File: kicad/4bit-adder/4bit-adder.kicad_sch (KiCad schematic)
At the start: 1 part, among them K1 SR11-5V-200-2C

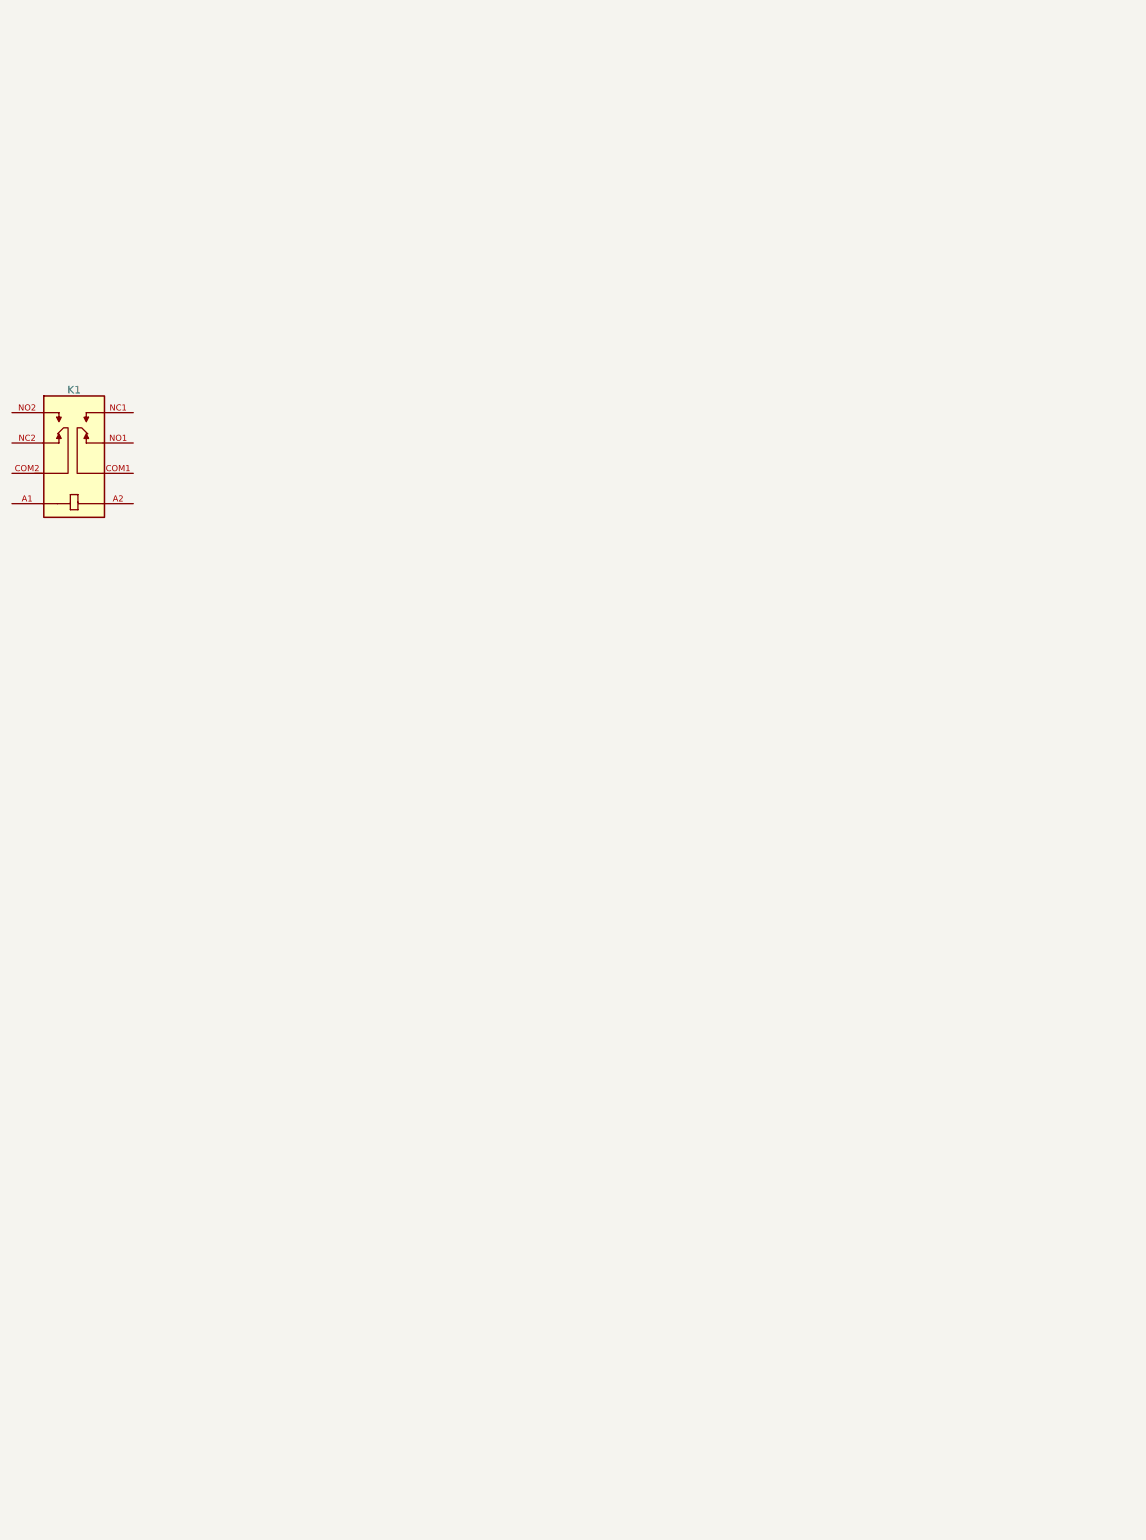
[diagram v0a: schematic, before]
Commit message: half adder schema
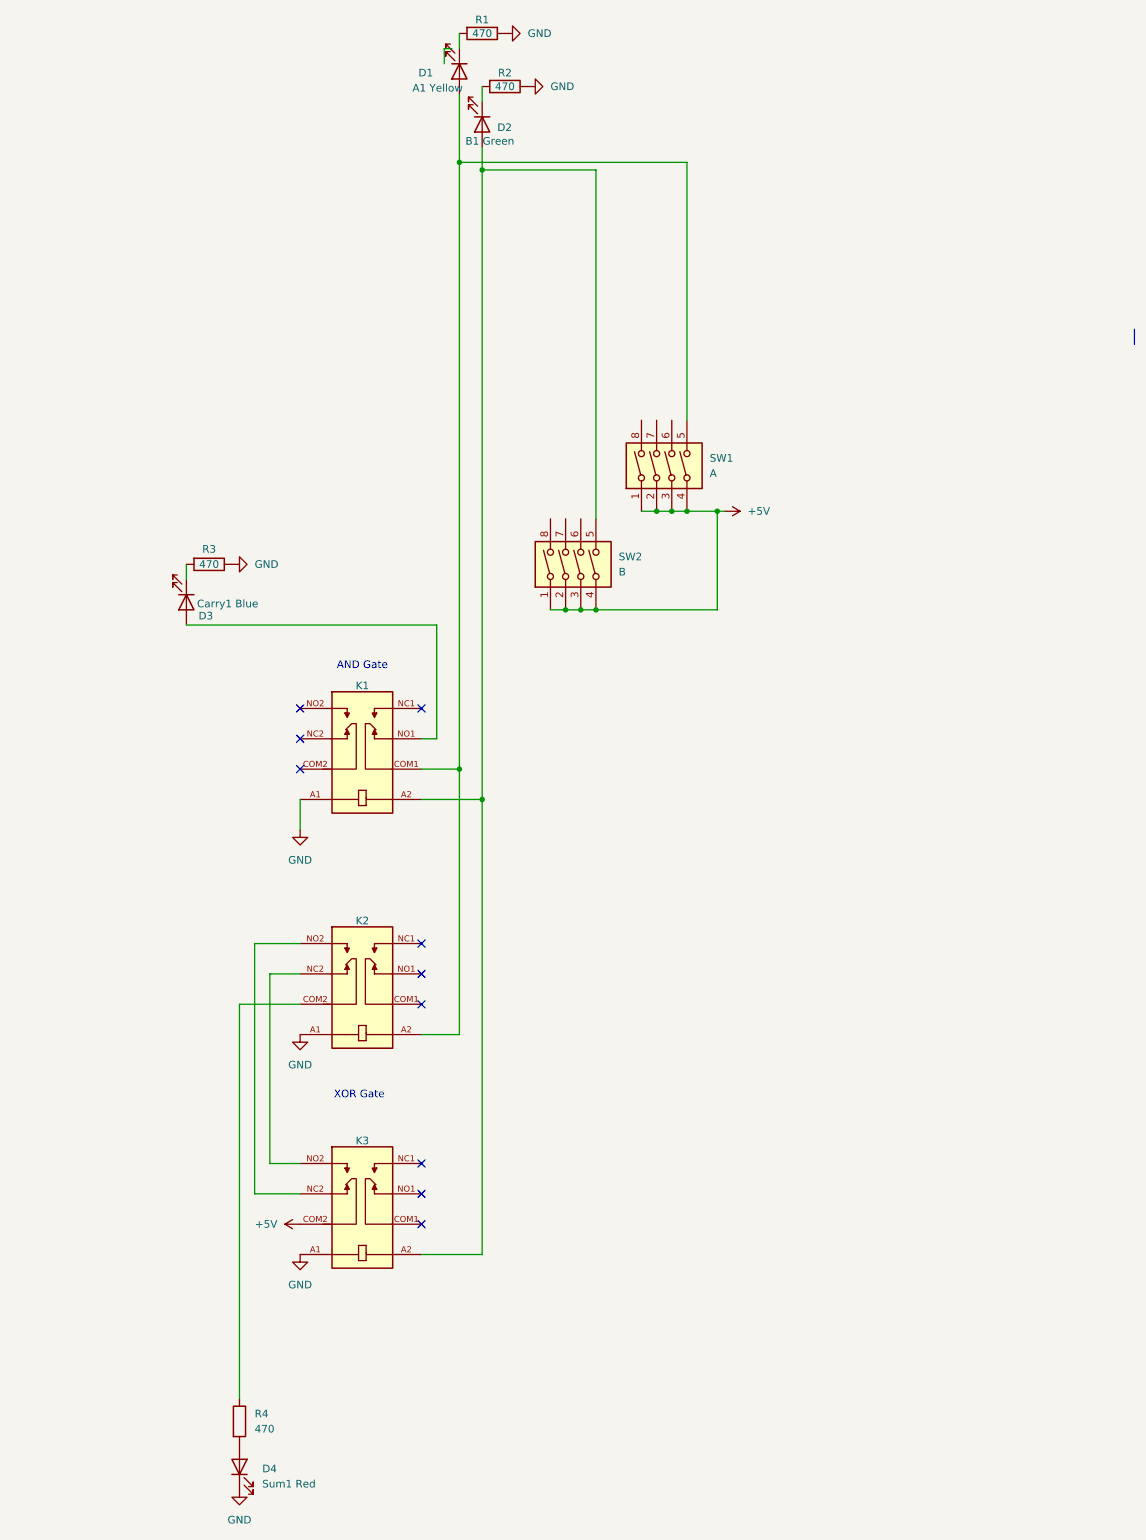
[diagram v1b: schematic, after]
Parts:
- added D1: A1 Yellow, LED_THT:LED_D5.0mm, symbol Device:LED
- added D2: B1 Green, LED_THT:LED_D5.0mm, symbol Device:LED
- added D3: Carry1 Blue, LED_THT:LED_D5.0mm, symbol Device:LED
- added D4: Sum1 Red, LED_THT:LED_D5.0mm, symbol Device:LED
- added K2, K3: SR11-5V-200-2C, SR11_5V_200_2C:RELAY_SR11-5V-200-2C, symbol SR11-5V-200-2C:SR11-5V-200-2C
- added R1, R2, R3, R4: 470, Resistor_THT:R_Axial_DIN0207_L6.3mm_D2.5mm_P10.16mm_Horizontal, symbol Device:R
- added SW1: A, Button_Switch_THT:SW_DIP_SPSTx04_Piano_10.8x11.72mm_W7.62mm_P2.54mm, symbol Switch:SW_DIP_x04
- added SW2: B, Button_Switch_THT:SW_DIP_SPSTx04_Piano_10.8x11.72mm_W7.62mm_P2.54mm, symbol Switch:SW_DIP_x04
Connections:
- net GND: now reaches K1.A1
- net GND: now also D4.1 (K), K2.A1, K3.A1, R1.1, R2.1, R3.1
- net at K1.A2: now also D2.2 (A), K3.A2, SW2.5
- net at K1.COM1: now also D1.2 (A), K2.A2, SW1.5
- net at K1.NO1: now also D3.2 (A)
- new net: D1.1 (K), R1.2
- new net: D2.1 (K), R2.2
- new net: K2.COM2, R4.1
- new net: K2.NC2, K3.NO2
- new net: K2.NO2, K3.NC2
- new net: D3.1 (K), R3.2
- new net: D4.2 (A), R4.2
- new net +5V: K3.COM2, SW1.1, SW1.2, SW1.3, SW1.4, SW2.1, SW2.2, SW2.3, SW2.4
- no-connect marks 0 -> 10
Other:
- note added: "AND Gate"
- note added: "XOR Gate"
- moved on the sheet: K1

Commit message: wip schema
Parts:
- removed D1: A1 Yellow, LED_THT:LED_D5.0mm, symbol Device:LED
- removed D3: Carry1 Blue, LED_THT:LED_D5.0mm, symbol Device:LED
- removed D4: Sum1 Red, LED_THT:LED_D5.0mm, symbol Device:LED
- removed K1, K2, K3: SR11-5V-200-2C, SR11_5V_200_2C:RELAY_SR11-5V-200-2C, symbol SR11-5V-200-2C:SR11-5V-200-2C
- removed R1, R3, R4: 470, Resistor_THT:R_Axial_DIN0207_L6.3mm_D2.5mm_P10.16mm_Horizontal, symbol Device:R
- removed SW1: A, Button_Switch_THT:SW_DIP_SPSTx04_Piano_10.8x11.72mm_W7.62mm_P2.54mm, symbol Switch:SW_DIP_x04
- removed SW2: B, Button_Switch_THT:SW_DIP_SPSTx04_Piano_10.8x11.72mm_W7.62mm_P2.54mm, symbol Switch:SW_DIP_x04
- added D1, D3, D4: 1N4007, Diode_THT:D_DO-41_SOD81_P10.16mm_Horizontal, symbol Diode:1N4007
- added D10: A4 Yellow, LED_THT:LED_D5.0mm, symbol Device:LED
- added D11: Carry2 White, LED_THT:LED_D5.0mm, symbol Device:LED
- added D12: Carry3 White, LED_THT:LED_D5.0mm, symbol Device:LED
- added D15: B4 Green, LED_THT:LED_D5.0mm, symbol Device:LED
- added D16: A3 Yellow, LED_THT:LED_D5.0mm, symbol Device:LED
- added D17: B3 Green, LED_THT:LED_D5.0mm, symbol Device:LED
- added D18: A2 Yellow, LED_THT:LED_D5.0mm, symbol Device:LED
- added D19: B2 Green, LED_THT:LED_D5.0mm, symbol Device:LED
- added D21: B1 Green, LED_THT:LED_D5.0mm, symbol Device:LED
- added D8: Sum1 Red, LED_THT:LED_D5.0mm, symbol Device:LED
- added D9: Carry1 White, LED_THT:LED_D5.0mm, symbol Device:LED
- added J1: Screw_Terminal_01x02, TerminalBlock:TerminalBlock_MaiXu_MX126-5.0-02P_1x02_P5.00mm, symbol Connector:Screw_Terminal_01x02
- added K1, K10, K11, K12, K13, K14, K15, K17, K18, K2, K3, K4, K5, K6: SR11-5V-200-2C-PH, SR11_5V_200_2C:RELAY_SR11-5V-200-2C, symbol SR11-5V-200-2C:SR11-5V-200-2C-PH
- added K7, K8, K9: SR11-5V-200-2C, SR11_5V_200_2C:RELAY_SR11-5V-200-2C, symbol SR11-5V-200-2C:SR11-5V-200-2C
- added R10, R15, R16, R17, R18, R19, R20, R21, R22, R23, R8: 470, Resistor_THT:R_Axial_DIN0207_L6.3mm_D2.5mm_P10.16mm_Horizontal, symbol Device:R
- added SW3: A, Button_Switch_THT:SW_DIP_SPSTx04_Piano_10.8x11.72mm_W7.62mm_P2.54mm, symbol Switch:SW_DIP_x04
- added SW4: B, Button_Switch_THT:SW_DIP_SPSTx04_Piano_10.8x11.72mm_W7.62mm_P2.54mm, symbol Switch:SW_DIP_x04
- D2: value B1 Green -> A1 Yellow
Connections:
- net +5V: now also J1.1 (Pin_1), K4.COM2, K6.COM2, K9.COM2, SW3.5, SW3.6, SW3.7, SW3.8, SW4.5, SW4.6, SW4.7, SW4.8
- net GND: now also J1.2 (Pin_2), K1.A1, K17.A1, K2.A1, K3.A1, K4.A1, K6.A1, K7.A1, K8.A1, K9.A1, R10.2, R15.2, R16.2, R17.2, R18.2, R19.2, R20.2, R21.2, R22.2, R23.2, R8.2
- net at D2.2 (A): now also K7.COM1, K8.A2, SW3.1
- new net: D19.1 (K), R19.1
- new net: D19.2 (A), K5.A2, SW4.2
- new net: D12.1 (K), R23.1
- new net: D8.1 (K), R8.1
- new net: D8.2 (A), K8.COM2
- new net: D15.1 (K), R15.1
- new net: D21.2 (A), K7.A2, K9.A2, SW4.1
- new net: D17.2 (A), SW4.3
- new net: K8.NO2, K9.NC2
- new net: K8.NC2, K9.NO2
- new net: D9.2 (A), K17.A2, K7.NC1
- new net: K5.A1, K6.A2
- new net: K4.NO2, K5.NC2
- new net: K4.NC2, K5.NO2
- new net: D11.1 (K), R22.1
- new net: D18.2 (A), K1.COM1, K2.COM1, K4.A2, SW3.2
- new net: D3.2 (A), K2.NO1
- new net: D9.1 (K), R20.1
- new net: D17.1 (K), R17.1
- new net: D10.1 (K), R10.1
- new net: D1.2 (A), K1.NO1
- new net: D16.1 (K), R16.1
- new net: K17.NC2, K6.NO2
- new net: K17.NO2, K6.NC2
- new net: D21.1 (K), R21.1
- new net: D4.2 (A), K3.NO1
- new net: D18.1 (K), R18.1
- new net: D16.2 (A), SW3.3
- no-connect marks 10 -> 30

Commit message: schematic first draft
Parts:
- removed K7, K8, K9: SR11-5V-200-2C, SR11_5V_200_2C:RELAY_SR11-5V-200-2C, symbol SR11-5V-200-2C:SR11-5V-200-2C
- added D13: Sum2 Red, LED_THT:LED_D5.0mm, symbol Device:LED
- added D14: Sum3 Red, LED_THT:LED_D5.0mm, symbol Device:LED
- added D20: Sum4 Red, LED_THT:LED_D5.0mm, symbol Device:LED
- added D22, D23, D24, D5, D6, D7: 1N4007, Diode_THT:D_DO-41_SOD81_P10.16mm_Horizontal, symbol Diode:1N4007
- added D25: Carry4 Red, LED_THT:LED_D5.0mm, symbol Device:LED
- added K16, K19, K20, K21, K22, K23, K24, K7, K8, K9: SR11-5V-200-2C-PH, SR11_5V_200_2C:RELAY_SR11-5V-200-2C, symbol SR11-5V-200-2C:SR11-5V-200-2C-PH
- added R11, R12, R13, R9: 470, Resistor_THT:R_Axial_DIN0207_L6.3mm_D2.5mm_P10.16mm_Horizontal, symbol Device:R
- added SW1: SW_Wuerth_450301014042, Button_Switch_THT:SW_Slide-03_Wuerth-WS-SLTV_10x2.5x6.4_P2.54mm, symbol Switch:SW_Wuerth_450301014042
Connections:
- net GND: now also K10.A1, K11.A1, K12.A1, K13.A1, K14.A1, K15.A1, K18.A1, K5.A1, K16.A1, K19.A1, K20.A1, K21.A1, K22.A1, K23.A1, K24.A1, K7.A1, K8.A1, K9.A1, R11.2, R12.2, R13.2, R9.2
- net at K18.A2: now also D1.1 (K), D11.2 (A), D3.1 (K), D4.1 (K), K11.A2, K12.A2
- net at K18.COM2: now also D14.2 (A)
- net at K18.NC2: now also K15.NO2
- net at K18.NO2: now also K15.NC2
- net at K10.A2: now also D17.2 (A), K12.COM1, K14.A2, SW4.3
- net at K10.COM1: now also D16.2 (A), K11.COM1, K13.A2, SW3.3
- net at K10.NO1: now also D5.2 (A)
- net at D19.2 (A), K5.A2, SW4.2: now also K1.A2, K3.COM1
- net at D12.2 (A): now also D5.1 (K), D6.1 (K), D7.1 (K), K19.A2, K20.A2, K24.A2
- net at D8.2 (A): now also K8.COM2
- net at D15.2 (A): now also SW4.4, K16.A2, K20.COM1, K22.A2
- net at K11.NO1: now also D6.2 (A)
- net at K15.A2: now also K14.COM2
- net SWV: now reaches K15.COM2
- net SWV: now also K13.COM2, K4.COM2, K6.COM2, SW3.5, SW3.6, SW3.7, SW3.8, SW4.5, SW4.6, SW4.7, SW4.8, K21.COM2, K23.COM2, K9.COM2, SW1.2 (C)
- net at D21.2 (A), SW4.1: now also K7.A2, K9.A2
- net at D2.2 (A), SW3.1: now also K7.COM1, K8.A2
- net at D9.2 (A), K17.A2: now also K2.A2, K3.A2, K7.NC1
- net at K6.A2: now also K5.COM2; no longer K5.A1
- net at K14.NC2: now also K13.NO2
- net at K14.NO2: now also K13.NC2
- net at D10.2 (A): now also SW3.4, K16.COM1, K19.COM1, K21.A2
- net at K17.COM2: now also D13.2 (A)
- net at K12.NO1: now also D7.2 (A)
- removed net +5V: J1.1 (Pin_1), K4.COM2, K6.COM2, SW3.5, SW3.6, SW3.7, SW3.8, SW4.5, SW4.6, SW4.7, SW4.8
- new net: D24.2 (A), K20.NO1
- new net: K21.NC2, K22.NO2
- new net: K21.NO2, K22.NC2
- new net: D14.1 (K), R11.1
- new net: J1.1 (Pin_1), SW1.1 (B)
- new net: D20.1 (K), R12.1
- new net: D20.2 (A), K24.COM2
- new net: D22.1 (K), D23.1 (K), D24.1 (K), D25.2 (A)
- new net: D22.2 (A), K16.NO1
- new net: K22.COM2, K23.A2
- new net: K23.NC2, K24.NO2
- new net: K23.NO2, K24.NC2
- new net: D13.1 (K), R9.1
- new net: D23.2 (A), K19.NO1
- new net: K8.NO2, K9.NC2
- new net: K8.NC2, K9.NO2
- new net: D25.1 (K), R13.1
- no-connect marks 30 -> 83

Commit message: initial pcb layout
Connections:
- net at D9.2 (A), K17.A2, K2.A2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: now also K7.NO1; no longer K7.NC1
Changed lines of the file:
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@@
+	)
+	(no_connect
+		(at 167.64 66.04)
 	)
 	(no_connect
@@
 	)
 	(no_connect
-		(at 167.64 60.96)
-	)
-	(no_connect
 		(at 167.64 119.38)
 	)
@@
 	(wire
 		(pts
-			(xy 167.64 66.04) (xy 168.91 66.04)
-		)
-		(stroke
-			(width 0)
-			(type default)
-		)
-	)
-	(wire
-		(pts
 			(xy 25.4 187.96) (xy 24.13 187.96)
 		)
@@
 	(wire
 		(pts
-			(xy 168.91 17.78) (xy 168.91 66.04)
+			(xy 168.91 17.78) (xy 168.91 60.96)
 		)
 		(stroke
@@
 		)
 		(stroke
+			(width 0)
+			(type default)
+		)
+	)
+	(wire
+		(pts
+			(xy 167.64 60.96) (xy 168.91 60.96)
+		)
+		(stroke

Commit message: footprints initial layout
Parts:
- added C1: 100uF, Capacitor_THT:CP_Radial_D10.0mm_P2.50mm, symbol Device:C_Polarized
- added D26, D27, D28, D29, D30, D31, D32, D33, D34, D35, D36, D37, D38, D39, D40, D41, D42, D43, D44, D45, D46, D47, D48, D49: 1N4001, Diode_THT:D_DO-41_SOD81_P10.16mm_Horizontal, symbol Diode:1N4003
- D1, D22, D23, D24, D3, D4, D5, D6, D7: value 1N4007 -> 1N4001
- D10, D11, D12, D13, D14, D15, D16, D17, D18, D19, D2, D20, D21, D25, D8, D9: footprint LED_THT:LED_D5.0mm -> LED_THT:LED_D3.0mm
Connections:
- net GND: now also K1.A2, K10.A2, K11.A2, K12.A2, K13.A2, K14.A2, K15.A2, K16.A2, K17.A2, K18.A2, K19.A2, K2.A2, K20.A2, K21.A2, K22.A2, K23.A2, K24.A2, K3.A2, K4.A2, K5.A2, K6.A2, K7.A2, K8.A2, K9.A2, C1.2, D26.2 (A), D27.2 (A), D28.2 (A), D29.2 (A), D30.2 (A), D31.2 (A), D32.2 (A), D33.2 (A), D34.2 (A), D35.2 (A), D36.2 (A), D37.2 (A), D38.2 (A), D39.2 (A), D40.2 (A), D41.2 (A), D42.2 (A), D43.2 (A), D44.2 (A), D45.2 (A), D46.2 (A), D47.2 (A), D48.2 (A), D49.2 (A); no longer K1.A1, K10.A1, K11.A1, K12.A1, K13.A1, K14.A1, K15.A1, K16.A1, K17.A1, K18.A1, K19.A1, K2.A1, K20.A1, K21.A1, K22.A1, K23.A1, K24.A1, K3.A1, K4.A1, K5.A1, K6.A1, K7.A1, K8.A1, K9.A1
- net SWV: now also SW3.1, SW3.2, SW3.3, SW3.4, SW4.1, SW4.2, SW4.3, SW4.4; no longer SW3.5, SW3.6, SW3.7, SW3.8, SW4.5, SW4.6, SW4.7, SW4.8
- net at D12.2 (A), D5.1 (K), D6.1 (K)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: now also K19.A1, K20.A1, K24.A1, D36.1 (K), D43.1 (K), D46.1 (K); no longer K19.A2, K20.A2, K24.A2
- net at D10.2 (A), K16.COM1, K19.COM1: now also K21.A1, SW3.8, D42.1 (K); no longer K21.A2, SW3.4
- net at D1.1 (K), D11.2 (A), D3.1 (K)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: now also K11.A1, K12.A1, K18.A1, D35.1 (K), D44.1 (K), D45.1 (K); no longer K11.A2, K12.A2, K18.A2
- net at K5.COM2: now also K6.A1, D49.1 (K); no longer K6.A2
- net at K14.COM2: now also K15.A1, D38.1 (K); no longer K15.A2
- net at J1.1 (Pin_1), SW1.1 (B): now also C1.1
- net at D18.2 (A), K1.COM1, K2.COM1: now also K4.A1, SW3.6, D32.1 (K); no longer K4.A2, SW3.2
- net at D16.2 (A), K10.COM1, K11.COM1: now also K13.A1, SW3.7, D41.1 (K); no longer K13.A2, SW3.3
- net at K22.COM2: now also K23.A1, D37.1 (K); no longer K23.A2
- net at D2.2 (A), K7.COM1: now also K8.A1, SW3.5, D27.1 (K); no longer K8.A2, SW3.1
- new net: D15.2 (A), D40.1 (K), D47.1 (K), K16.A1, K20.COM1, K22.A1, SW4.8
- new net: D19.2 (A), D29.1 (K), D33.1 (K), K1.A1, K3.COM1, K5.A1, SW4.6
- new net: D17.2 (A), D39.1 (K), D48.1 (K), K10.A1, K12.COM1, K14.A1, SW4.7
- new net: D30.1 (K), D31.1 (K), D34.1 (K), D9.2 (A), K17.A1, K2.A1, K3.A1, K7.NO1
- new net: D21.2 (A), D26.1 (K), D28.1 (K), K7.A1, K9.A1, SW4.5
